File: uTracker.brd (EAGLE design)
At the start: 19.1 x 71.1 mm, 30 parts, among them J1 ICSP, U2 LTC3526BEDCPBF, U3 ATMEGA328P

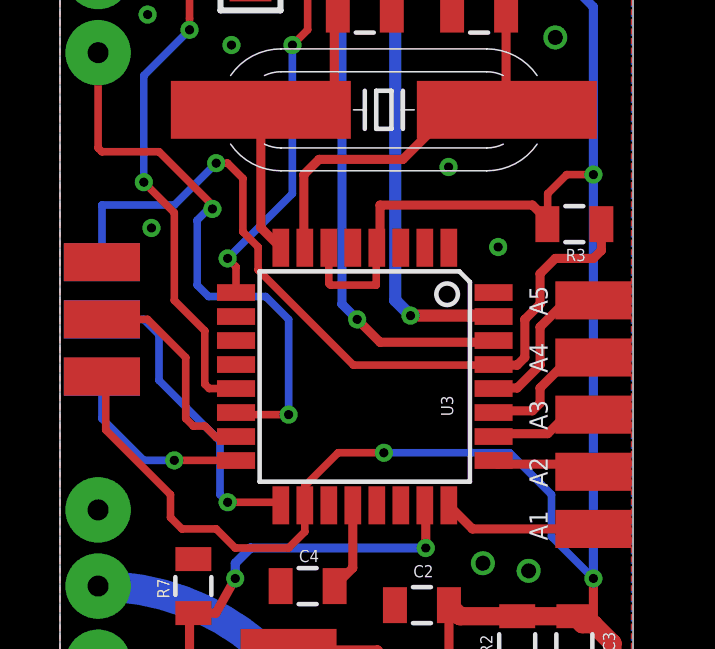
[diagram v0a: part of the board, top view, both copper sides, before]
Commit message: Modified ICSP header to match 0.1" spacing
This should ease programming by allowing a standard 2x3 0.1" header to
be clipped on the side of the board.
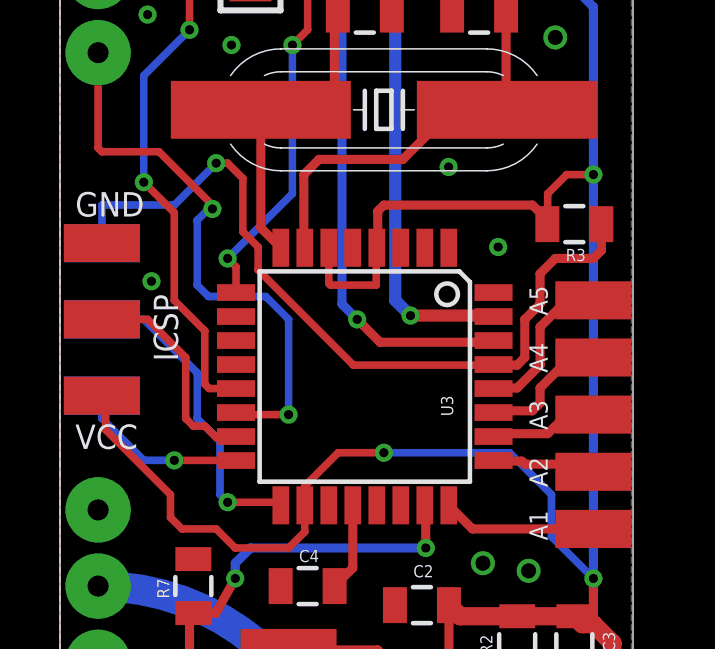
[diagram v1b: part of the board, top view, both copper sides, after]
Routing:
- net RESET: track 27.2 -> 26.6 mm
- net MISO: track 6.45 -> 5.81 mm
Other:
- board text added: "GND"
- board text added: "ICSP"
- board text added: "MISO"
- board text added: "RST"
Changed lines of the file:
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@@
 <setting verticaltext="up"/>
 </settings>
-<grid distance="0.05" unitdist="inch" unit="mm" style="lines" multiple="1" display="yes" altdistance="0.005" altunitdist="inch" altunit="mm"/>
+<grid distance="0.05" unitdist="inch" unit="mil" style="lines" multiple="1" display="yes" altdistance="1" altunitdist="mil" altunit="mil"/>
 <layers>
 <layer number="1" name="Top" color="4" fill="1" visible="yes" active="yes"/>
@@
 </polygon>
 <rectangle x1="11.303" y1="54.864" x2="15.621" y2="67.31" layer="22"/>
+<text x="7.747" y="20.193" size="0.8128" layer="21" font="vector" ratio="20" rot="R90">ICSP</text>
+<text x="6.35" y="25.019" size="0.8128" layer="22" font="vector" ratio="20" rot="MR0">RST</text>
+<text x="6.731" y="17.272" size="0.8128" layer="22" font="vector" ratio="20" rot="MR0">MISO</text>
+<text x="4.318" y="17.272" size="0.8128" layer="21" font="vector" ratio="20">VCC</text>
+<text x="4.318" y="25.019" size="0.8128" layer="21" font="vector" ratio="20">GND</text>
 </plain>
 <attributes>
@@
 <via x="20.066" y="41.656" extent="1-16" drill="0.5" diameter="0.254"/>
 <via x="6.731" y="31.75" extent="1-16" drill="0.3048"/>
-<via x="6.858" y="24.638" extent="1-16" drill="0.3048"/>
+<via x="6.858" y="22.86" extent="1-16" drill="0.3048"/>
 <via x="17.907" y="13.462" extent="1-16" drill="0.5" diameter="0.254"/>
 <via x="19.431" y="13.208" extent="1-16" drill="0.5" diameter="0.254"/>
@@
 <wire x1="19.295" y1="35.805" x2="19.295" y2="36.96" width="0.3048" layer="1"/>
 <wire x1="14.37" y1="23.9776" x2="14.478" y2="24.0856" width="0.3048" layer="1"/>
-<wire x1="14.478" y1="24.0856" x2="14.478" y2="25.4" width="0.3048" layer="1"/>
-<wire x1="14.478" y1="25.4" x2="19.558" y2="25.4" width="0.3048" layer="1"/>
 <wire x1="19.558" y1="25.4" x2="20.055" y2="24.903" width="0.3048" layer="1"/>
 <wire x1="20.055" y1="24.903" x2="20.055" y2="24.765" width="0.3048" layer="1"/>
@@
 <wire x1="7.493" y1="15.748" x2="5.334" y2="17.907" width="0.254" layer="1"/>
 <wire x1="5.334" y1="17.907" x2="5.334" y2="19.431" width="0.254" layer="1"/>
-<wire x1="5.334" y1="19.431" x2="5.207" y2="19.685" width="0.254" layer="1"/>
+<wire x1="5.334" y1="19.431" x2="5.207" y2="19.05" width="0.254" layer="1"/>
 <wire x1="12.77" y1="23.9776" x2="12.77" y2="22.79" width="0.254" layer="1"/>
 <wire x1="12.77" y1="22.79" x2="12.827" y2="22.733" width="0.254" layer="1"/>
@@
 <wire x1="9.144" y1="39.624" x2="10.4195" y2="38.3485" width="0.4064" layer="1"/>
 <wire x1="10.4195" y1="38.3485" x2="10.4195" y2="38.0945" width="0.4064" layer="1"/>
+<wire x1="19.558" y1="25.4" x2="14.605" y2="25.4" width="0.3048" layer="1"/>
+<wire x1="14.605" y1="25.4" x2="14.4018" y2="25.1968" width="0.3048" layer="1"/>
+<wire x1="14.4018" y1="25.1968" x2="14.4018" y2="24.0094" width="0.3048" layer="1"/>
+<wire x1="14.4018" y1="24.0094" x2="14.37" y2="23.9776" width="0.3048" layer="1"/>
 </signal>
 <signal name="N$3">
@@
 <wire x1="9.398" y1="15.494" x2="9.144" y2="15.748" width="0.254" layer="16"/>
 <wire x1="9.144" y1="15.748" x2="9.144" y2="17.526" width="0.254" layer="16"/>
-<wire x1="9.144" y1="17.526" x2="7.112" y2="19.558" width="0.254" layer="16"/>
-<wire x1="7.112" y1="19.558" x2="7.112" y2="21.082" width="0.254" layer="16"/>
-<wire x1="7.112" y1="21.082" x2="6.604" y2="21.59" width="0.254" layer="16"/>
+<wire x1="9.144" y1="17.526" x2="8.382" y2="18.288" width="0.254" layer="16"/>
+<wire x1="8.382" y1="18.288" x2="8.382" y2="19.812" width="0.254" layer="16"/>
+<wire x1="8.382" y1="19.812" x2="6.604" y2="21.59" width="0.254" layer="16"/>
 <wire x1="6.604" y1="21.59" x2="5.207" y2="21.59" width="0.254" layer="16"/>
 </signal>
@@
 <wire x1="7.62" y1="16.891" x2="6.604" y2="16.891" width="0.254" layer="16"/>
 <wire x1="6.604" y1="16.891" x2="5.207" y2="18.288" width="0.254" layer="16"/>
-<wire x1="5.207" y1="18.288" x2="5.207" y2="19.685" width="0.254" layer="16"/>
+<wire x1="5.207" y1="18.288" x2="5.207" y2="19.05" width="0.254" layer="16"/>
 </signal>
 <signal name="MOSI">
@@
 <wire x1="21.59" y1="23.622" x2="21.855" y2="23.887" width="0.3048" layer="1"/>
 <wire x1="21.855" y1="23.887" x2="21.855" y2="24.765" width="0.3048" layer="1"/>
-<wire x1="5.207" y1="23.495" x2="5.207" y2="25.4" width="0.254" layer="16"/>
+<wire x1="5.207" y1="24.13" x2="5.207" y2="25.4" width="0.254" layer="16"/>
 <wire x1="5.207" y1="25.4" x2="7.62" y2="25.4" width="0.254" layer="16"/>
 <wire x1="7.62" y1="25.4" x2="9.017" y2="26.797" width="0.254" layer="16"/>
@@
 <contactref element="EXP" pad="2"/>
 <wire x1="18.2626" y1="16.885" x2="18.3836" y2="16.764" width="0.3048" layer="1"/>
-<wire x1="18.3836" y1="16.764" x2="21.082" y2="16.764" width="0.3048" layer="1"/>
 <wire x1="21.082" y1="16.764" x2="21.336" y2="16.51" width="0.3048" layer="1"/>
 <wire x1="21.336" y1="16.51" x2="21.59" y2="16.51" width="0.3048" layer="1"/>
+<wire x1="21.082" y1="16.764" x2="19.304" y2="16.764" width="0.3048" layer="1"/>
+<wire x1="19.304" y1="16.764" x2="19.2024" y2="16.8656" width="0.3048" layer="1"/>
+<wire x1="19.2024" y1="16.8656" x2="18.282" y2="16.8656" width="0.3048" layer="1"/>
+<wire x1="18.282" y1="16.8656" x2="18.2626" y2="16.885" width="0.3048" layer="1"/>
 </signal>
 <signal name="A3">
